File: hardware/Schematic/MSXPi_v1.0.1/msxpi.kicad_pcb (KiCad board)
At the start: 2 copper layers, 103 x 66 mm, 39 parts, among them IC1 LD117A, J1 ROM_SWITCH, U1 AT28C256

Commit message: v1.0.1 Rev 1 - Added some silk that was missing
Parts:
- moved G*** 6.70 mm to (136.2, 80.3)
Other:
- board text added: "How to Write the EEPROM ======================= The ROM file may be 16K or 32K. 1. Remove jumps CS1, CS2, CS12 2. Boot the MSX into DOS 3. Add jumpers CS12, WR, SLTSL 4. Run at28c256.com /s <slot> /f <filename> To boot ROM 1: Add jumpers CS1,A15 To boot RoM 2: dd jumpers CS1, A14"
- board text added: "V1.0.1 Rev 1"
- board text removed: "How to Write the EEPROM ======================= The ROM file may be 32K or 64K. 1. Remove jumps CS1, CS2, CS12 2. Boot the MSX into DOS 3. Add jumpers CS12, WR, SLTSL 4. Run at28c256.com /s <slot> /f <filename> To boot ROM 1: Add jumpers CS1,A15 To boot RoM 2: dd jumpers CS1, A14"
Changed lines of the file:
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@@
       (effects (font (size 1.143 1.143) (thickness 0.127)) (justify left bottom))
     )
-    (fp_text value "470" (at -1.5748 2.794) (layer "F.SilkS")
+    (fp_text value "470" (at -1.8868 0.5622) (layer "F.SilkS")
       (effects (font (size 1.143 1.143) (thickness 0.127)) (justify left bottom))
     )
@@
       (effects (font (size 1 1) (thickness 0.15)))
     )
-    (fp_text value "AT28C256" (at 7.493 15.5956) (layer "F.Fab")
+    (fp_text value "AT28C256" (at -2.249 4.15 180) (layer "F.SilkS")
       (effects (font (size 1 1) (thickness 0.15)))
     )
@@
       (effects (font (size 1.143 1.143) (thickness 0.127)) (justify left bottom))
     )
-    (fp_text value "100uf" (at 2.1336 -4.0132 180) (layer "F.SilkS")
+    (fp_text value "100uf" (at -2.54 0 180) (layer "F.SilkS")
       (effects (font (size 1.143 1.143) (thickness 0.127)) (justify left bottom))
     )
@@
       (effects (font (size 1.6002 1.6002) (thickness 0.1778)) (justify left bottom))
     )
-    (fp_text value "EPM3064ALC44" (at 0 -11.938) (layer "F.Fab") hide
-      (effects (font (size 1.6002 1.6002) (thickness 0.1778)) (justify left bottom))
+    (fp_text value "EPM3064ALC44" (at -12.680881 -11.856651) (layer "F.SilkS")
+      (effects (font (size 1.2 1.2) (thickness 0.1778)) (justify left bottom))
     )
     (fp_line (start 8.255 4.699) (end 10.414 4.699) (layer "F.SilkS") (width 0.1524))
@@
   )
   (footprint "LOGO" (layer "F.Cu")
-    (at 142.7734 81.8134)
+    (at 136.246151 80.290038)
     (attr board_only exclude_from_pos_files exclude_from_bom)
     (fp_text reference "G***" (at 0 0) (layer "F.SilkS") hide
@@
   (gr_rect (start 157.502616 76.789373) (end 155.019611 74.329044) (layer "User.2") (width 0.1) (fill none))
   (gr_rect (start 193.04 76.708) (end 187.994625 74.219326) (layer "User.2") (width 0.1) (fill none))
-  (gr_text "How to Write the EEPROM\n=======================\n\n\n\nThe ROM file may be 32K or 64K.\n\n1. Remove jumps CS1, CS2, CS12\n2. Boot the MSX into DOS\n3. Add jumpers CS12, WR, SLTSL\n4. Run at28c256.com /s <slot> /f <filename>\n\nTo boot ROM 1: Add jumpers CS1,A15\nTo boot RoM 2: dd jumpers CS1, A14" (at 192.6082 91.0844) (layer "B.SilkS")
-    (effects (font (size 0.7 0.7) (thickness 0.125)) (justify left mirror))
+  (gr_text "How to Write the EEPROM\n=======================\nThe ROM file may be 16K or 32K.\n\n1. Remove jumps CS1, CS2, CS12\n2. Boot the MSX into DOS\n3. Add jumpers CS12, WR, SLTSL\n4. Run at28c256.com /s <slot> /f <filename>\nTo boot ROM 1: Add jumpers CS1,A15\nTo boot RoM 2: dd jumpers CS1, A14" (at 192.5 90) (layer "B.SilkS")
+    (effects (font (size 1.4 1.4) (thickness 0.25)) (justify left mirror))
   )
   (gr_text "GND" (at 188.976 77.590457) (layer "F.SilkS")
     (effects (font (size 1 1) (thickness 0.15)))
   )
-  (gr_text "https://github.com/costarc/MSXPi" (at 158.0642 81.7372) (layer "F.SilkS")
-    (effects (font (size 1 1) (thickness 0.125)))
+  (gr_text "https://github.com/costarc/MSXPi" (at 158.1823 80.230911) (layer "F.SilkS")
+    (effects (font (size 1.5 1.5) (thickness 0.125)))
   )
   (gr_text "CLK" (at 148.8694 77.597) (layer "F.SilkS")
@@
     (effects (font (size 1.5 1.5) (thickness 0.3)))
   )
+  (gr_text "V1.0.1 Rev 1" (at 195 125) (layer "F.SilkS")
+    (effects (font (size 1 1) (thickness 0.15)))
+  )
   (gr_text "/CS12" (at 191.0588 94.9706) (layer "F.SilkS")

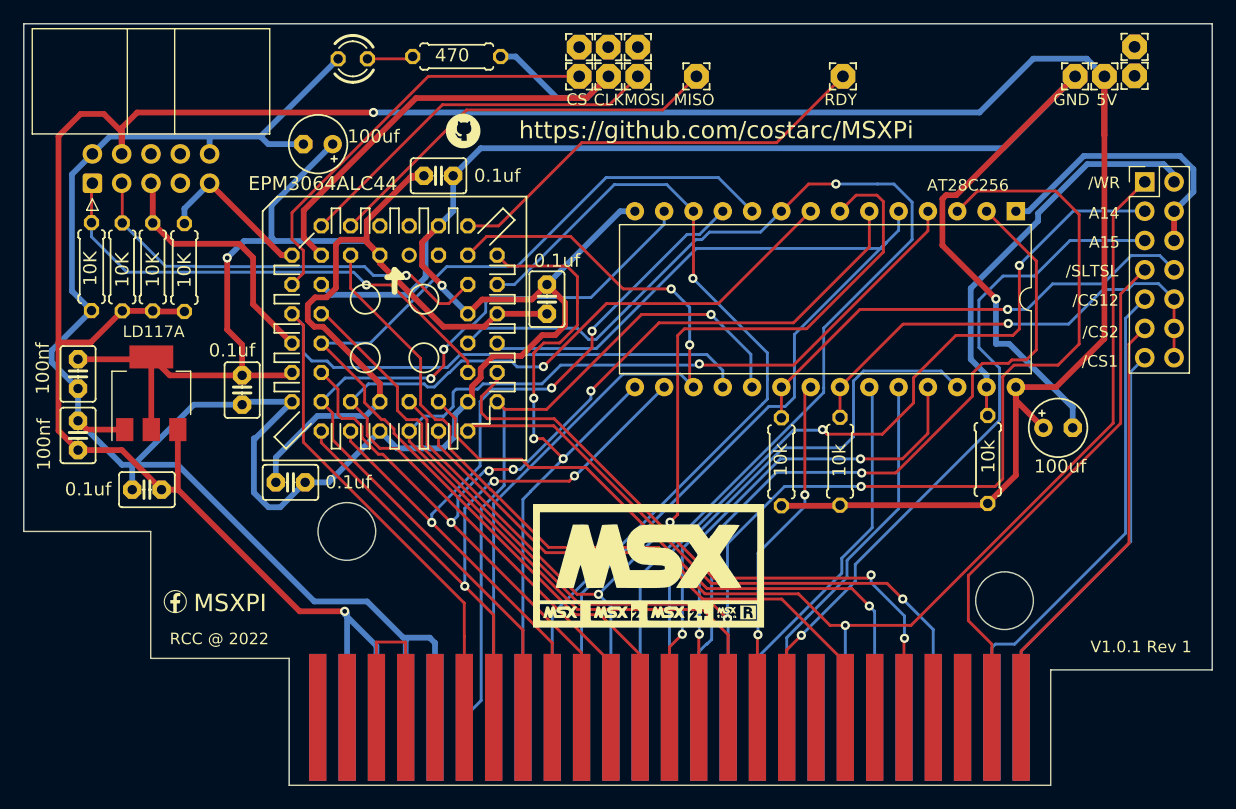
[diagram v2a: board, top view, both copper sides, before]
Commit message: Minimnized jumpers - SLTSL and A14/A15 only
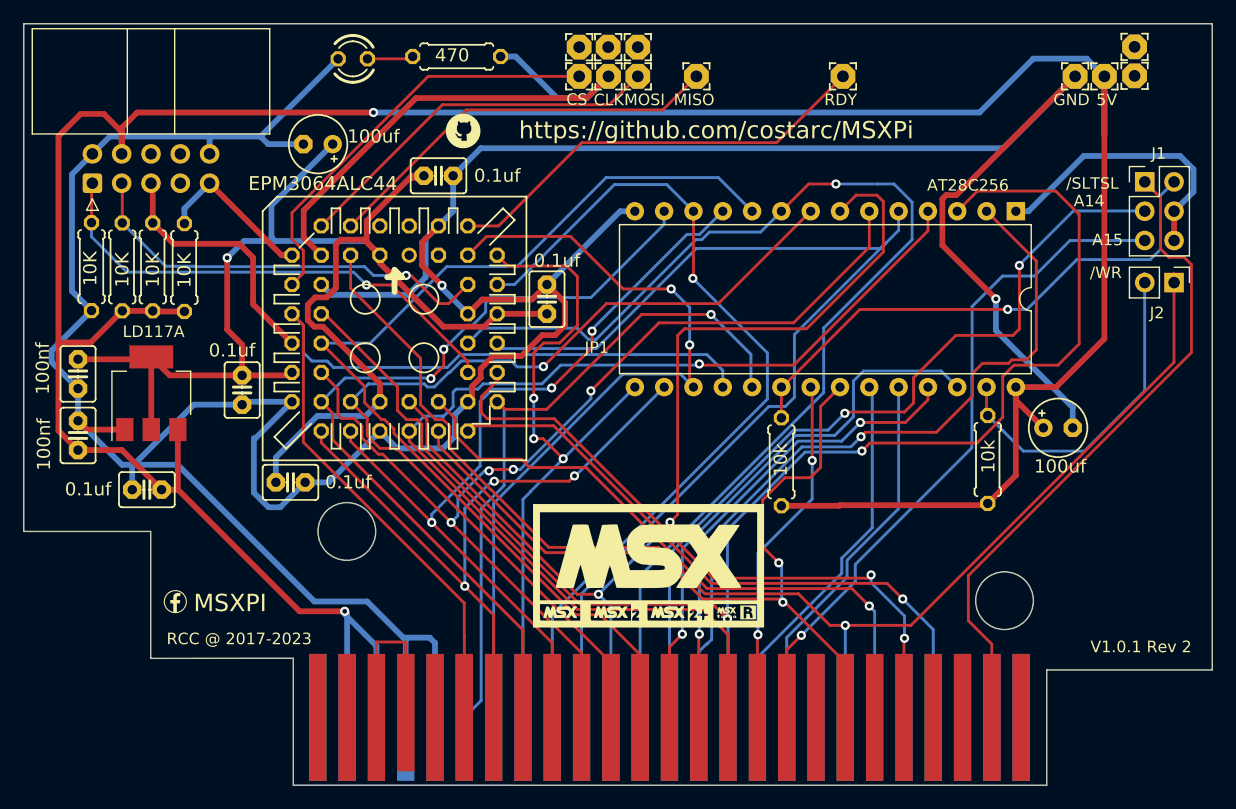
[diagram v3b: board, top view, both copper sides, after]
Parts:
- removed R6: 10k, msxpi:0207_7
- added J2: WRITE_EN, Connector_PinHeader_2.54mm:PinHeader_1x02_P2.54mm_Vertical, F.Cu at (197.9, 93.4)
- J1: footprint Connector_PinHeader_2.54mm:PinHeader_2x07_P2.54mm_Vertical -> Connector_PinHeader_2.54mm:PinHeader_2x03_P2.54mm_Vertical
- JP1: footprint Roni Footprints:MSX_CART -> Roni Footprints:MSX_CART_SW
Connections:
- J1 pad 1: /WR -> /SLTSL
- J1 pad 2: /MEM_WE -> /MEM_CE
- U1 pad 22: /MEM_OE -> /RD
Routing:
- net /CS12: track 42.7 -> 0.00 mm
- net /MEM_OE: track 41.0 -> 0.00 mm, vias 1 -> 0
- net /CS2: track 38.1 -> 0.00 mm
- net /CS1: track 35.6 -> 0.00 mm
- net /RD: track 49.0 -> 72.5 mm, vias 0 -> 2
- net /SLTSL: track 46.0 -> 57.7 mm
- net /WR: track 121.8 -> 115.0 mm
- net /MEM_WE: track 35.1 -> 29.8 mm
- net /MEM_CE: track 41.9 -> 46.9 mm
- net A7: track 129.8 -> 127.4 mm
- net A8: track 43.1 -> 41.4 mm
- net A15: track 61.1 -> 59.6 mm
- net A13: track 48.7 -> 47.7 mm
- net GNDREF: track 329.7 -> 329.1 mm
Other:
- outline, holes or cut-outs redrawn
- board text added: "RCC @ 2017-2023"
- board text added: "V1.0.1 Rev 2"
- board text removed: "/CS1"
- board text removed: "/CS12"
- board text removed: "/CS2"
- board text removed: "RCC @ 2022"
- board text removed: "V1.0.1 Rev 1"

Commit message: Updated footprint to r1 (smaller size & 3 holes)- better fit for Patola case
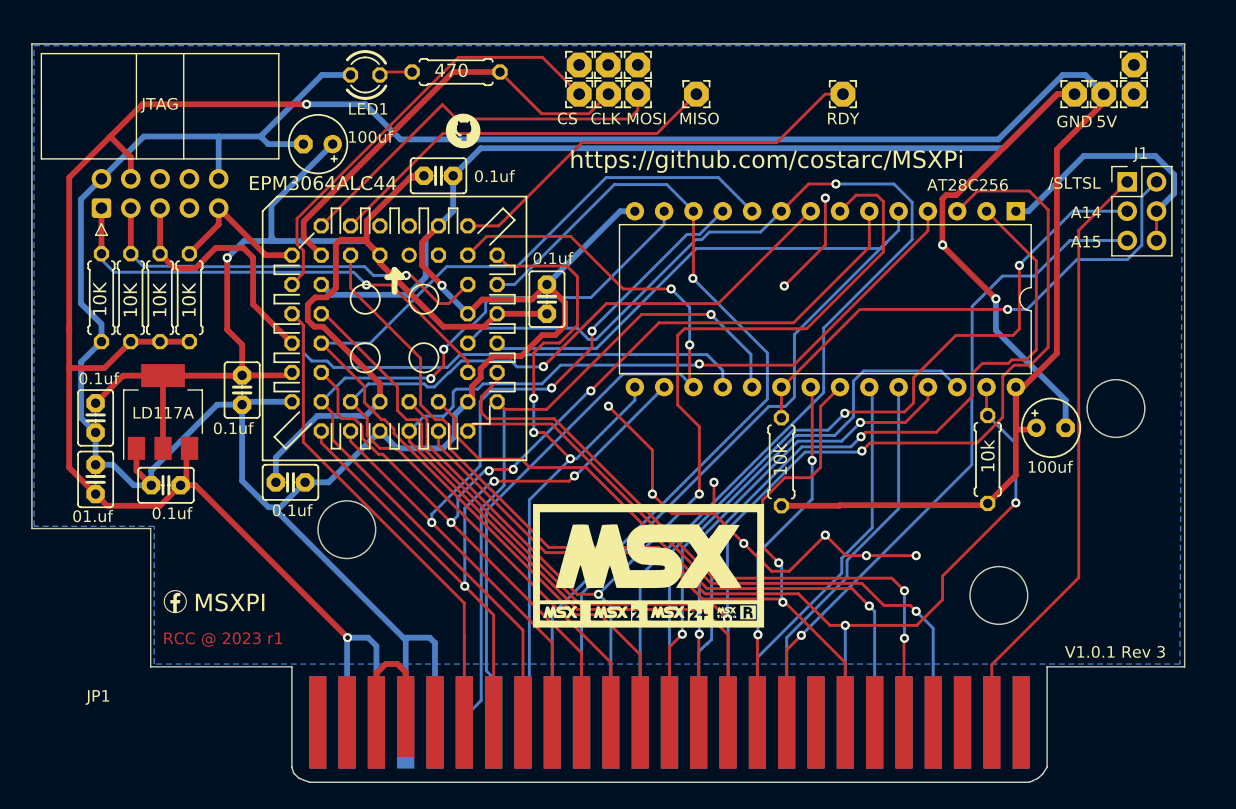
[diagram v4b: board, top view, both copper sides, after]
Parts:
- removed J2: WRITE_EN, Connector_PinHeader_2.54mm:PinHeader_1x02_P2.54mm_Vertical
- C1: value 100nf -> 01.uf
- C3: value 100nf -> 0.1uf
- JP1: footprint Roni Footprints:MSX_CART_SW -> Roni Footprints:MSX_CART_SW_Official_3Holes
- moved C3 4.10 mm to (104.4, 105.2)
- moved C1 4.10 mm to (104.4, 110.5)
- moved R1 2.83 mm to (104.9, 94.7)
- moved R2 2.77 mm to (107.4, 94.7)
- moved R3 2.74 mm to (110.0, 94.7)
- moved R4 2.65 mm to (112.5, 94.7)
- moved JP2 2.30 mm to (104.9, 87.0)
- moved IC1 1.92 mm to (110.2, 104.6)
- moved LED1 1.77 mm to (127.8, 75.4)
- moved C6 1.69 mm to (110.5, 111.0)
- moved MOUNTHOLE4 1.59 mm to (194.4, 77.1)
- moved MOUNTHOLE5 1.57 mm to (194.4, 74.6)
- moved GND5 1.54 mm to (189.2, 77.1)
- moved +5V1 1.54 mm to (191.8, 77.1)
- moved SPI_CLK_PI_GPIO1 1.54 mm to (148.8, 77.1)
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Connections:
- R5 pad 1: /MEM_WE -> /WR
- U1 pad 27: /MEM_WE -> /WR
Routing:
- net GNDREF: track 329.1 -> 360.5 mm, vias 2 -> 12
- net /MEM_WE: track 29.8 -> 0.00 mm
- net /WR: track 115.0 -> 100.8 mm, vias 1 -> 2
- net +5V: track 263.5 -> 252.4 mm
- net SPI_CLK: track 47.4 -> 37.5 mm
- net /SLTSL: track 57.7 -> 51.3 mm
- net A7: track 127.4 -> 122.4 mm
- net Net-(JP1-Pad44): track 15.6 -> 11.3 mm
- net MEM_A14: track 24.7 -> 22.7 mm
- net TCK: track 42.7 -> 40.8 mm
- net /MEM_CE: track 46.9 -> 45.1 mm
- net A3: track 90.7 -> 92.3 mm
- net A14: track 72.2 -> 70.7 mm
- net A15: track 59.6 -> 58.1 mm
- net +3.3V: track 127.8 -> 126.3 mm
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- added copper zone on B.Cu, net GNDREF
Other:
- board size 103 x 66 mm -> 99.9 x 64 mm
- board text added: "1. Remove jumper /SLT 2. Boot into MSX-DOS 3. Close jumper /SLT and A15 4. Run: at28c256.com /s <slot> /f <filename> To boot ROM 1: Close jumper /SLT & A15 To boot ROM 2: Close jumper /SLT & A14"
- board text added: "How to Write the EEPROM ======================= The ROM file may be 8/16/32KB."
- board text added: "V1.0.1 Rev 3"
- board text removed: "/WR"
- board text removed: "How to Write the EEPROM ======================= The ROM file may be 16K or 32K. 1. Remove jumps CS1, CS2, CS12 2. Boot the MSX into DOS 3. Add jumpers CS12, WR, SLTSL 4. Run at28c256.com /s <slot> /f <filename> To boot ROM 1: Add jumpers CS1,A15 To boot RoM 2: dd jumpers CS1, A14"
- board text removed: "RCC @ 2017-2023"
- board text removed: "V1.0.1 Rev 2"
